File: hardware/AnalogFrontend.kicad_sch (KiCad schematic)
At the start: 27 parts, among them J2 Exp1, J3 Exp2, J4 Exp3, J5 Exp4, U4 AD7718, U5 AD7718, Y1 MS1V-T1K-32.768kHz-12.5pF-20P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, Y2 MS1V-T1K-32.768kHz-12.5pF-20P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

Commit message: added mouser part numbers
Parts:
- C10: Notes (none) -> im Uni-Sortiment?; Part Source (none) -> Uni
- C11, C13, C14, C15, C16, C18, C20, C21, C22, C9, R10, R44, R45, R59, R7, R8, R9: Part Source (none) -> Uni
- C17: footprint Capacitor_SMD:C_1210_3225Metric -> Capacitor_SMD:C_0805_2012Metric; Notes (none) -> im Uni-Sortiment?; Part Source (none) -> Uni
- J2: value Exp1 -> AudioJack; Mouser No (none) -> 568-NMJ6HFD2-AU; Part Source (none) -> Mouser
- J3: value Exp2 -> AudioJack; Mouser No (none) -> 568-NMJ6HFD2-AU; Part Source (none) -> Mouser
- J4: value Exp3 -> AudioJack; Mouser No (none) -> 568-NMJ6HFD2-AU; Part Source (none) -> Mouser
- J5: value Exp4 -> AudioJack; Mouser No (none) -> 568-NMJ6HFD2-AU; Part Source (none) -> Mouser
- U4, U5: value AD7718 -> AD7718BRZ; Mouser No (none) -> 584-AD7718BRZ; Part Source (none) -> Mouser
- Y1, Y2: Mouser No (none) -> 428-200120-ML02; Notes (none) -> TODO: footpring; Part Source (none) -> Mouser

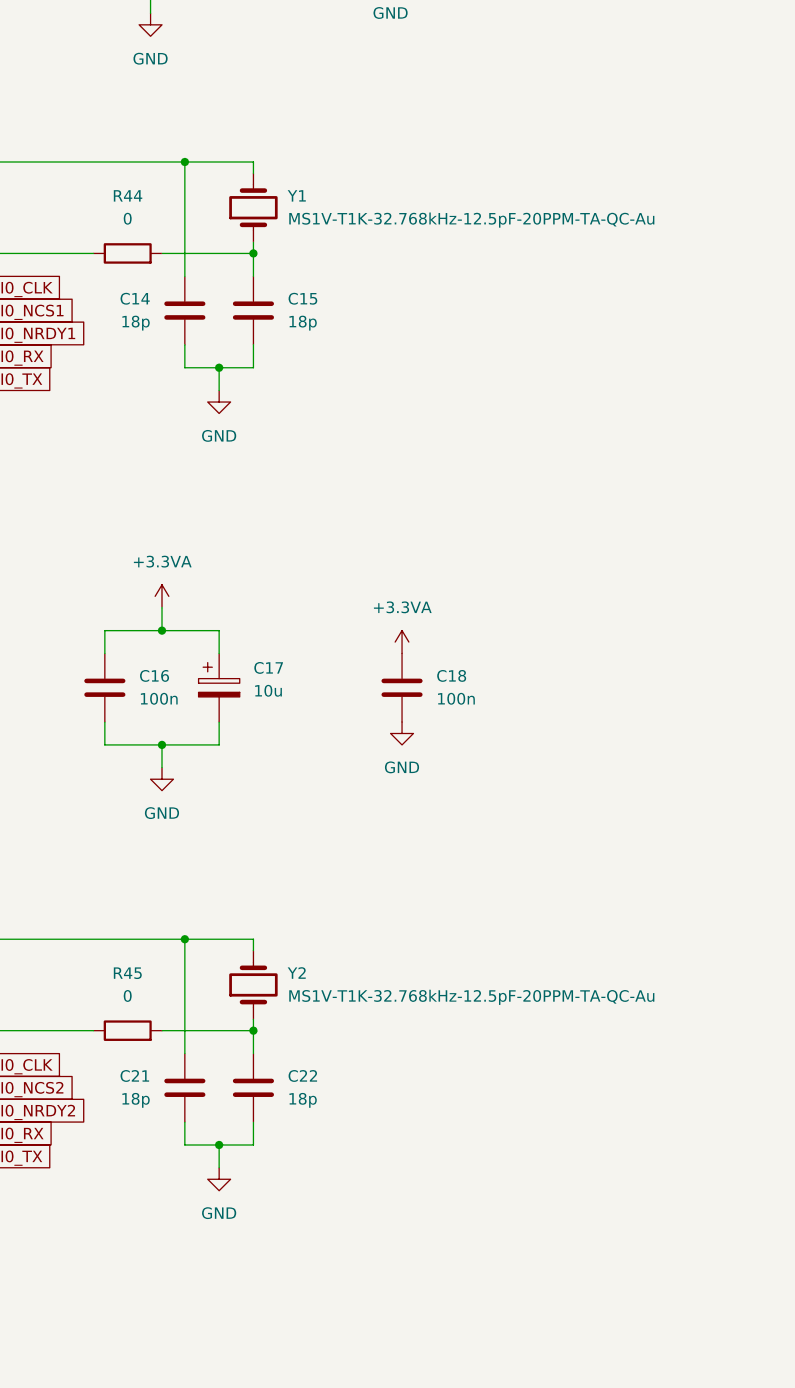
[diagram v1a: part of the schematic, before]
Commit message: added all footprints and parts
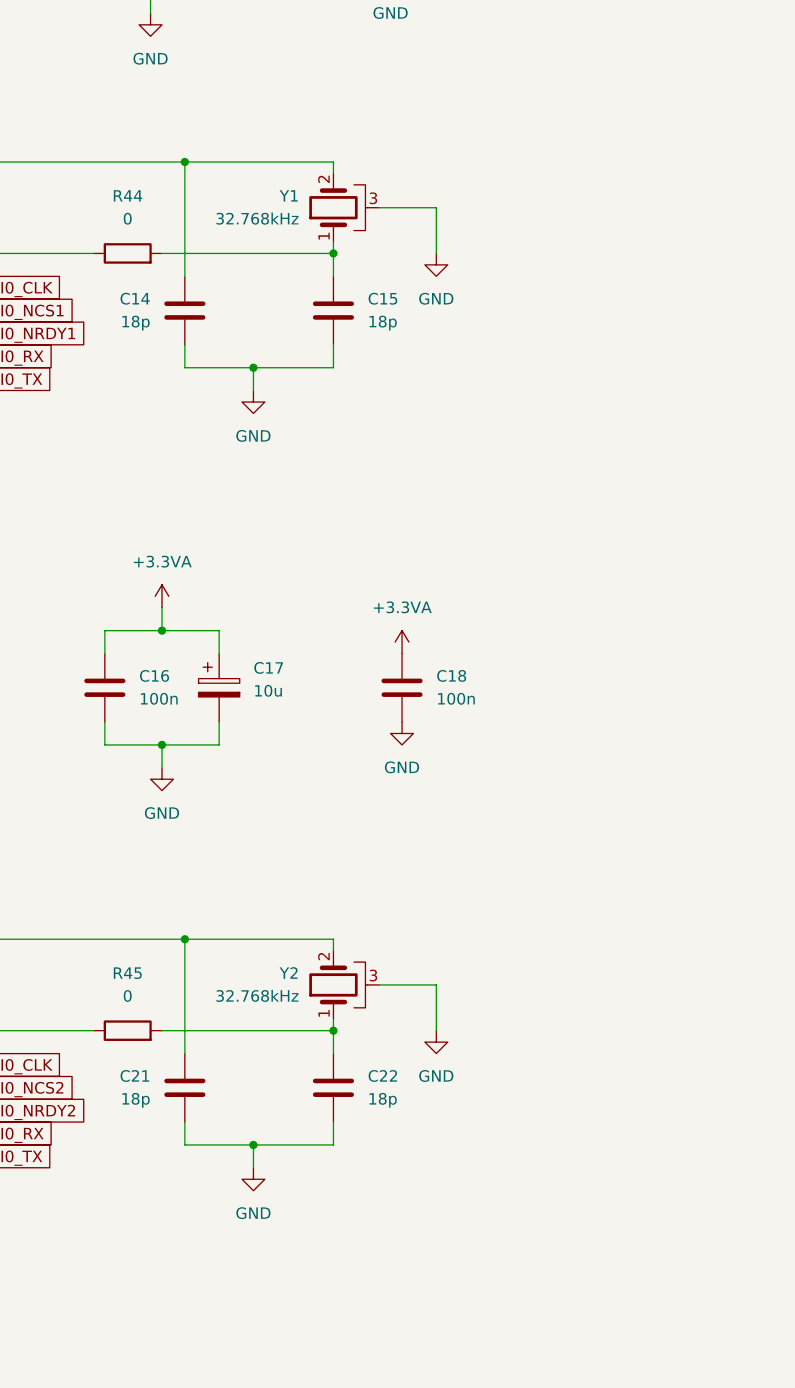
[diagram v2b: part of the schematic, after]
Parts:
- Y1, Y2: value MS1V-T1K-32.768kHz-12.5pF-20PPM-TA-QC-Au -> 32.768kHz; footprint Crystal:Crystal_SMD_3215-2Pin_3.2x1.5mm -> MS1V-T1K:MS1V-T1K; symbol Device:Crystal -> Device:Crystal_GND3; Notes TODO: footpring -> TODO: footprint
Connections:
- net AGND: now also Y1.3, Y2.3
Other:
- moved on the sheet: C15, C22

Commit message: more routing
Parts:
- Y1, Y2: Notes TODO: footprint -> (none)
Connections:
- net at C14.1, U4.28 (XTAL1): now also Y1.1; no longer Y1.2
- net at C15.1, R44.2: now also Y1.2; no longer Y1.1
- net at C22.1, R45.2: now also Y2.2; no longer Y2.1
- net at C21.1, U5.28 (XTAL1): now also Y2.1; no longer Y2.2
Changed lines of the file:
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@@
 		(lib_id "Device:Crystal_GND3")
 		(at 318.77 91.44 90)
+		(mirror x)
 		(unit 1)
 		(body_style 1)
@@
 		(in_pos_files yes)
 		(dnp no)
-		(fields_autoplaced yes)
 		(property "Reference" "Y1"
-			(at 314.96 90.1699 90)
+			(at 314.96 92.7101 90)
 			(show_name no)
 			(do_not_autoplace no)
@@
 		)
 		(property "Value" "32.768kHz"
-			(at 314.96 92.7099 90)
+			(at 314.96 90.1701 90)
 			(show_name no)
 			(do_not_autoplace no)
@@
 			)
 		)
-		(property "Notes" "TODO: footprint"
+		(property "Notes" ""
 			(at 318.77 91.44 90)
 			(hide yes)
@@
 		(lib_id "Device:Crystal_GND3")
 		(at 318.77 177.8 90)
+		(mirror x)
 		(unit 1)
 		(body_style 1)
@@
 		(in_pos_files yes)
 		(dnp no)
-		(fields_autoplaced yes)
 		(property "Reference" "Y2"
-			(at 314.96 176.5299 90)
+			(at 314.96 179.0701 90)
 			(show_name no)
 			(do_not_autoplace no)
@@
 		)
 		(property "Value" "32.768kHz"
-			(at 314.96 179.0699 90)
+			(at 314.96 176.5301 90)
 			(show_name no)
 			(do_not_autoplace no)
@@
 			)
 		)
-		(property "Notes" "TODO: footprint"
+		(property "Notes" ""
 			(at 318.77 177.8 90)
 			(hide yes)

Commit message: more routing progress
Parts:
- removed R59: 47, Resistor_SMD:R_0805_2012Metric, symbol Device:R
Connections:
- no-connect marks 12 -> 13

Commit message: added signed declaration and updated schematic names
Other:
- company: (none) -> Amon Benson, TU Berlin
- title: (none) -> Analog Front End
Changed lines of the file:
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@@
 	(generator_version "10.0")
 	(paper "A3")
+	(title_block
+		(title "Analog Front End")
+		(date "2026-09-27")
+		(rev "1.0")
+		(company "Amon Benson, TU Berlin")
+	)
 	(junction
 		(at 318.77 96.52)
